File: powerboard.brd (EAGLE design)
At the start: 0 parts

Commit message: place some parts
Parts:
- added BAT1+, BAT1-: (no value), wirepad:2,54/0,9
- added RPROG: 27k, rcl:R0402
- added U1: MCP73831T-2DCI/MC, MCP73831T-2DCI_MC:SON50P200X300X100-9N
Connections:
- new net EXP: U1.9
- new net GND: BAT1-.1, RPROG.1, U1.6
- new net N$1: RPROG.2, U1.8
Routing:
- net GND: track 0.00 -> 12.0 mm
- net N$1: track 0.00 -> 5.00 mm
- added copper zone on layer 16, net GND
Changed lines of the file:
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@@
 <drawing>
 <settings>
-<setting alwaysvectorfont="no"/>
+<setting alwaysvectorfont="yes"/>
 <setting verticaltext="up"/>
 </settings>
@@
 <layer number="51" name="tDocu" color="7" fill="1" visible="yes" active="yes"/>
 <layer number="52" name="bDocu" color="7" fill="1" visible="yes" active="yes"/>
+<layer number="90" name="Modules" color="5" fill="1" visible="no" active="no"/>
+<layer number="91" name="Nets" color="2" fill="1" visible="no" active="no"/>
+<layer number="92" name="Busses" color="1" fill="1" visible="no" active="no"/>
+<layer number="93" name="Pins" color="2" fill="1" visible="no" active="no"/>
+<layer number="94" name="Symbols" color="4" fill="1" visible="no" active="no"/>
+<layer number="95" name="Names" color="7" fill="1" visible="no" active="no"/>
+<layer number="96" name="Values" color="7" fill="1" visible="no" active="no"/>
+<layer number="97" name="Info" color="7" fill="1" visible="no" active="no"/>
+<layer number="98" name="Guide" color="6" fill="1" visible="no" active="no"/>
 </layers>
 <board>
@@
 </autorouter>
 <elements>
+<element name="U1" library="MCP73831T-2DCI_MC" package="SON50P200X300X100-9N" value="MCP73831T-2DCI/MC" x="11.43" y="16.51" smashed="yes">
+<attribute name="AVAILABILITY" value="In Stock" x="11.43" y="16.51" size="1.778" layer="27" display="off"/>
+<attribute name="DESCRIPTION" value=" Tiny Integrated Li-Ion/Li-Poly Charge mgnt controller, 4.2V Vreg out " x="11.43" y="16.51" size="1.778" layer="27" display="off"/>
+<attribute name="MF" value="Microchip" x="11.43" y="16.51" size="1.778" layer="27" display="off"/>
+<attribute name="MP" value="MCP73831T-2DCI/MC" x="11.43" y="16.51" size="1.778" layer="27" display="off"/>
+<attribute name="NAME" x="8.201" y="18.4" size="1.27" layer="25"/>
+<attribute name="PACKAGE" value="VFDFN-8 Microchip" x="11.43" y="16.51" size="1.778" layer="27" display="off"/>
+<attribute name="PRICE" value="None" x="11.43" y="16.51" size="1.778" layer="27" display="off"/>
+<attribute name="PURCHASE-URL" value="https://pricing.snapeda.com/search/part/MCP73831T-2DCI/MC/?ref=eda" x="11.43" y="16.51" size="1.778" layer="27" display="off"/>
+<attribute name="VALUE" x="8.201" y="14.747" size="1.27" layer="27" align="top-left"/>
+</element>
+<element name="BAT1+" library="wirepad" library_urn="urn:adsk.eagle:library:412" package="2,54/0,9" package3d_urn="urn:adsk.eagle:package:30847/1" value="" x="19.05" y="8.89" smashed="yes">
+<attribute name="NAME" x="17.78" y="10.414" size="1.27" layer="25" ratio="10"/>
+<attribute name="POPULARITY" value="2" x="19.05" y="8.89" size="1.778" layer="27" display="off"/>
+<attribute name="VALUE" x="19.05" y="9.49" size="0.0254" layer="27"/>
+</element>
+<element name="BAT1-" library="wirepad" library_urn="urn:adsk.eagle:library:412" package="2,54/0,9" package3d_urn="urn:adsk.eagle:package:30847/1" value="" x="15.24" y="8.89" smashed="yes">
+<attribute name="NAME" x="13.97" y="10.414" size="1.27" layer="25" ratio="10"/>
+<attribute name="POPULARITY" value="2" x="15.24" y="8.89" size="1.778" layer="27" display="off"/>
+<attribute name="VALUE" x="15.24" y="9.49" size="0.0254" layer="27"/>
+</element>
+<element name="RPROG" library="rcl" library_urn="urn:adsk.eagle:library:334" package="R0402" package3d_urn="urn:adsk.eagle:package:23547/3" value="27k" x="16.51" y="17.78" smashed="yes">
+<attribute name="NAME" x="15.875" y="18.415" size="1.27" layer="25"/>
+<attribute name="POPULARITY" value="34" x="16.51" y="17.78" size="1.778" layer="27" display="off"/>
+<attribute name="SPICEPREFIX" value="R" x="16.51" y="17.78" size="1.778" layer="27" display="off"/>
+<attribute name="VALUE" x="15.875" y="15.875" size="1.27" layer="27"/>
+</element>
 </elements>
 <signals>
+<signal name="EXP">
+<contactref element="U1" pad="9"/>
+</signal>
+<signal name="GND">
+<contactref element="U1" pad="6"/>
+<contactref element="BAT1-" pad="1"/>
+<polygon width="0.1524" layer="16" isolate="0.4064">
+<vertex x="0" y="29.21"/>
+<vertex x="63.5" y="29.21"/>
+<vertex x="63.5" y="1.27"/>
+<vertex x="1.27" y="1.27"/>
+<vertex x="0" y="2.54"/>
+</polygon>
+<contactref element="RPROG" pad="1"/>
+<wire x1="14.7828" y1="17.6784" x2="16.002" y2="17.6784" width="0.1524" layer="1"/>
+<wire x1="13.4112" y1="16.3068" x2="14.7828" y2="17.6784" width="0.1524" layer="1"/>
+<wire x1="12.954" y1="16.3068" x2="13.4112" y2="16.3068" width="0.1524" layer="1"/>
+<wire x1="16.002" y1="17.6784" x2="16.01" y2="17.78" width="0.1524" layer="1"/>
+<wire x1="12.954" y1="16.3068" x2="12.865" y2="16.26" width="0.1524" layer="1"/>
+<wire x1="15.24" y1="14.478" x2="13.4112" y2="16.3068" width="0.1524" layer="1"/>
+<wire x1="15.24" y1="8.89" x2="15.24" y2="14.478" width="0.1524" layer="1"/>
+</signal>
+<signal name="N$1">
+<contactref element="U1" pad="8"/>
+<contactref element="RPROG" pad="2"/>
+<wire x1="16.6116" y1="18.1356" x2="16.9164" y2="17.8308" width="0.1524" layer="1"/>
+<wire x1="16.6116" y1="18.288" x2="16.6116" y2="18.1356" width="0.1524" layer="1"/>
+<wire x1="16.4592" y1="18.4404" x2="16.6116" y2="18.288" width="0.1524" layer="1"/>
+<wire x1="14.0208" y1="18.4404" x2="16.4592" y2="18.4404" width="0.1524" layer="1"/>
+<wire x1="12.954" y1="17.3736" x2="14.0208" y2="18.4404" width="0.1524" layer="1"/>
+<wire x1="16.9164" y1="17.8308" x2="17.01" y2="17.78" width="0.1524" layer="1"/>
+<wire x1="12.954" y1="17.3736" x2="12.865" y2="17.26" width="0.1524" layer="1"/>
+</signal>
 </signals>
 <mfgpreviewcolors>
@@
 </board>
 </drawing>
+<compatibility>
+<note version="8.2" severity="warning">
+Since Version 8.2, EAGLE supports online libraries. The ids
+of those online libraries will not be understood (or retained)
+with this version.
+</note>
+<note version="8.3" severity="warning">
+Since Version 8.3, EAGLE supports URNs for individual library
+assets (packages, symbols, and devices). The URNs of those assets
+will not be understood (or retained) with this version.
+</note>
+<note version="8.3" severity="warning">
+Since Version 8.3, EAGLE supports the association of 3D packages
+with devices in libraries, schematics, and board files. Those 3D
+packages will not be understood (or retained) with this version.
+</note>
+</compatibility>
 </eagle>

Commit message: progress
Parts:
- added 3V3OUT, 5V-IN, BAT2+, BAT2-, BAT3+, BAT3-, GND-IN, GNDOUT: (no value), wirepad:2,54/0,9
- added C1, C2: 4.7uF, rcl:C0402
- added C3: 10uF, rcl:C0402
- added C4: 22uF, rcl:C0402
- added IC1: ISL9122AIRNZ-T, ISL9122AIRNZ-T:SON50P300X200X100-9N
- added JUMPER: 0, rcl:R0805
- added L1: (no value), rcl:L0201
- added LED1: (no value), led:CHIPLED_0603
- added LEDCURRENT: 0, rcl:R2512
- added R2: (no value), rcl:RTRIMCVR42A
- added RPROG1: 470, rcl:R0402
- added U$1: CHIPLED, samsung_chipled:CHIPLED2828
- added U2: MIC826RYMT-TR, mic826rymt-tr:UDFN6_HKA_MCH
- moved BAT1- 29.5 mm to (42.4, 20.3)
- moved BAT1+ 16.8 mm to (31.3, 20.3)
- moved RPROG 1.27 mm to (15.2, 17.8), turned to 90 degrees
- moved U1 1.27 mm to (11.4, 17.8)
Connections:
- removed net EXP: U1.9
- new net 3.3REGULATED: 3V3OUT.1, C4.1, IC1.4, LEDCURRENT.1
- new net 5VIN: 5V-IN.1, C1.1, U1.1, U1.2
- new net BAT_IN: C3.1, IC1.8, JUMPER.2, U2.6
- new net INDUCTOR1: IC1.3, L1.1
- new net INDUCTOR2: IC1.1, L1.2
- new net JUMPER: BAT1+.1, BAT2+.1, BAT3+.1, C2.1, JUMPER.1, U1.3, U1.4
- new net LED+: R2.2, U$1.ANODE
- new net N$10: IC1.5, U2.1
- new net N$2: LEDCURRENT.2, R2.3
- new net N$4: LED1.A, U1.5
- new net N$5: LED1.C, RPROG1.2
- net GND: now also BAT2-.1, BAT3-.1, C1.2, C2.2, C3.2, C4.2, GND-IN.1, GNDOUT.1, IC1.2, IC1.6, IC1.7, IC1.9, RPROG1.1, U$1.CATHODE, U1.9, U2.2, U2.7
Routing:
- net GND: track 12.0 -> 0.00 mm
- net N$1: track 5.00 -> 0.00 mm
- added copper zone on layer 1, net GND

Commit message: progress
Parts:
- C1, C2, C3, C4: device rcl:C0402 -> rcl:C0603K
- L1: value (none) -> 1uf; device rcl:L0201 -> vishayinductor:IND_IHHP-0806ZH-01_VIS
- moved L1 0.61 mm to (7.91, 11.6), turned to 270 degrees
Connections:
- net INDUCTOR1: now also L1.2; no longer L1.1
- net INDUCTOR2: now also L1.1; no longer L1.2
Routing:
- net JUMPER: track 0.00 -> 83.7 mm
- net 3.3REGULATED: track 0.00 -> 27.2 mm
- net BAT_IN: track 0.00 -> 20.0 mm
- net 5VIN: track 0.00 -> 9.13 mm
- net N$10: track 0.00 -> 5.75 mm
- net N$2: track 0.00 -> 4.76 mm
- net LED+: track 0.00 -> 4.17 mm
- net N$4: track 0.00 -> 3.65 mm
- net N$5: track 0.00 -> 3.00 mm
- net N$1: track 0.00 -> 2.48 mm
- net INDUCTOR2: track 0.00 -> 2.16 mm

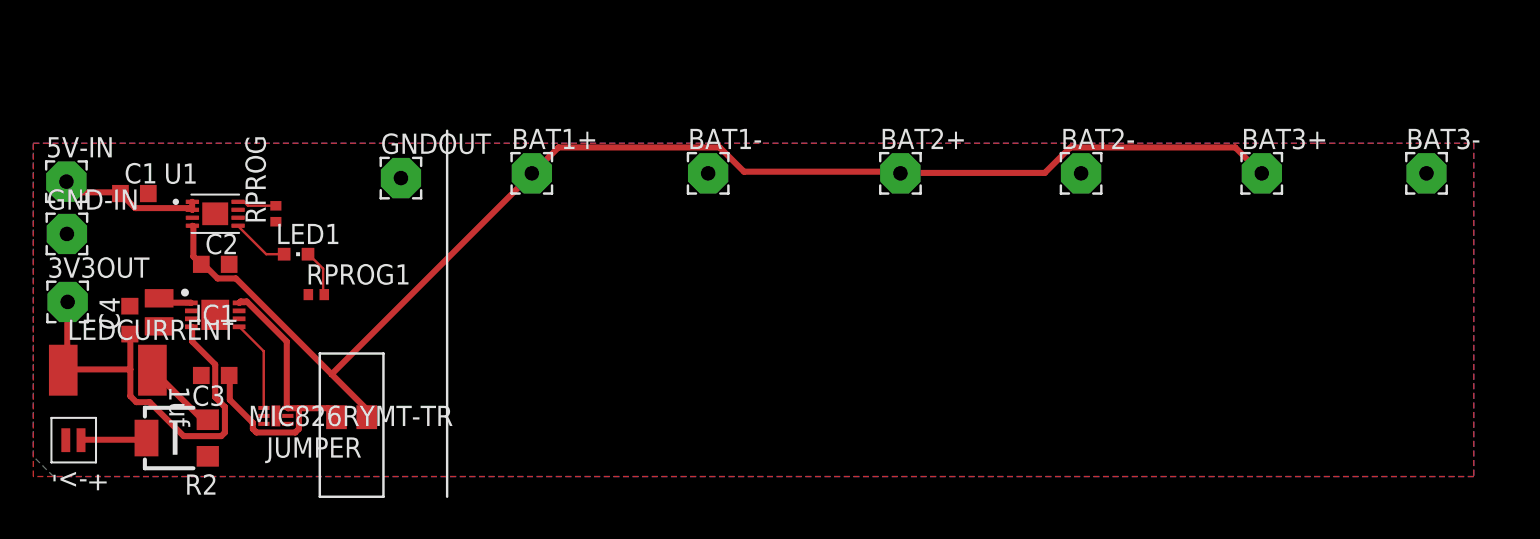
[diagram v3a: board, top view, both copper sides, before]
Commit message: add jlc rules, edit mic826 footprint
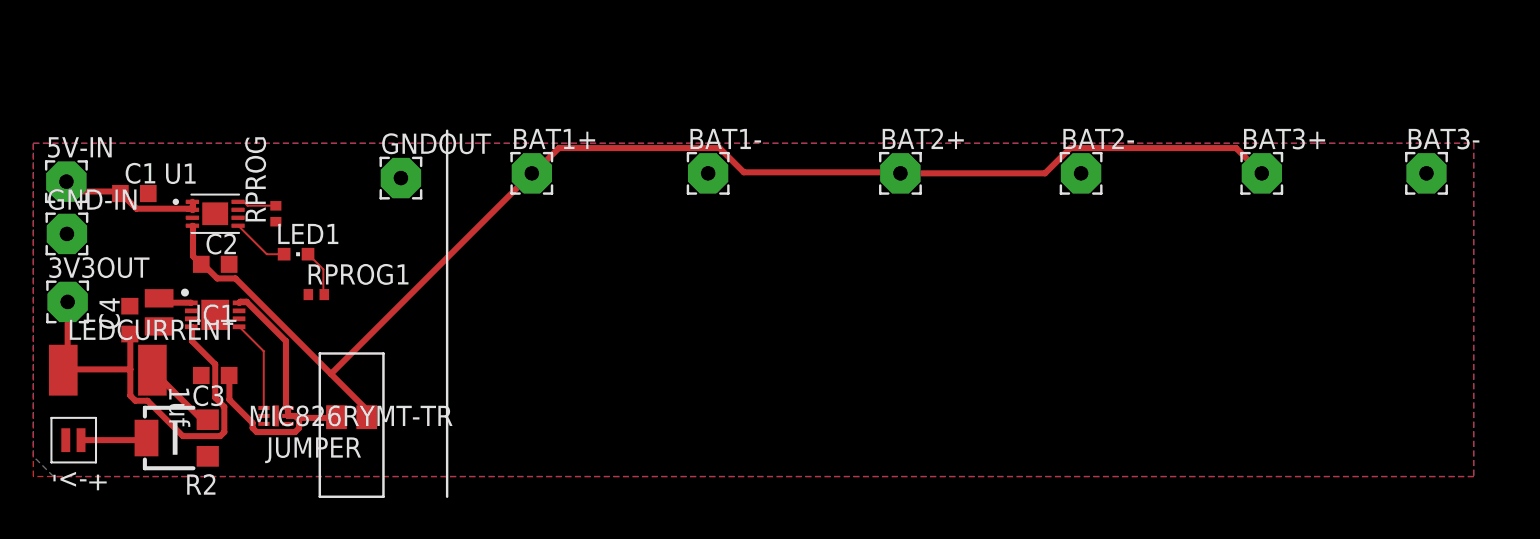
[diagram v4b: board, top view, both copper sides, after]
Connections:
- net BAT_IN: now also U2.5

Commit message: finish
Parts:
- moved C3 4.78 mm to (14.5, 11.3), turned to 270 degrees
- moved U2 2.72 mm to (13.7, 7.32)
- moved U$1 1.89 mm to (4.32, 4.19)
- moved R2 1.67 mm to (10.6, 3.75)
- moved C4 1.00 mm to (5.78, 12.1), turned to 270 degrees
- moved L1 0.39 mm to (8.29, 11.7)
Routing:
- net BAT_IN: track 19.6 -> 12.8 mm
- net 3.3REGULATED: track 27.1 -> 33.6 mm
- net N$10: track 5.75 -> 2.88 mm
- net INDUCTOR1: track 0.00 -> 1.81 mm
- net N$2: track 4.77 -> 6.41 mm
- net GND: track 0.00 -> 1.61 mm
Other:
- board outline added: 90 x 21 mm
